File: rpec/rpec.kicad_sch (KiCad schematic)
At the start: 31 parts, among them J1 GPIO, J10 Conn_02x04_Odd_Even, J11 Conn_02x04_Odd_Even, J12 Conn_02x03_Odd_Even, J2 Conn_01x02_Pin, J3 Conn_01x03_Pin, J4 Conn_02x03_Odd_Even, J5 Conn_01x04_Male, J6 Conn_01x04_Male, J7 Conn_01x03_Pin, J8 Conn_01x03_Pin, J9 Conn_01x04_Pin, M1 Fan, U1 CAT24C256, U2 PCF8563T, U3 MCP3428x-xSL, Y1 Crystal_GND3

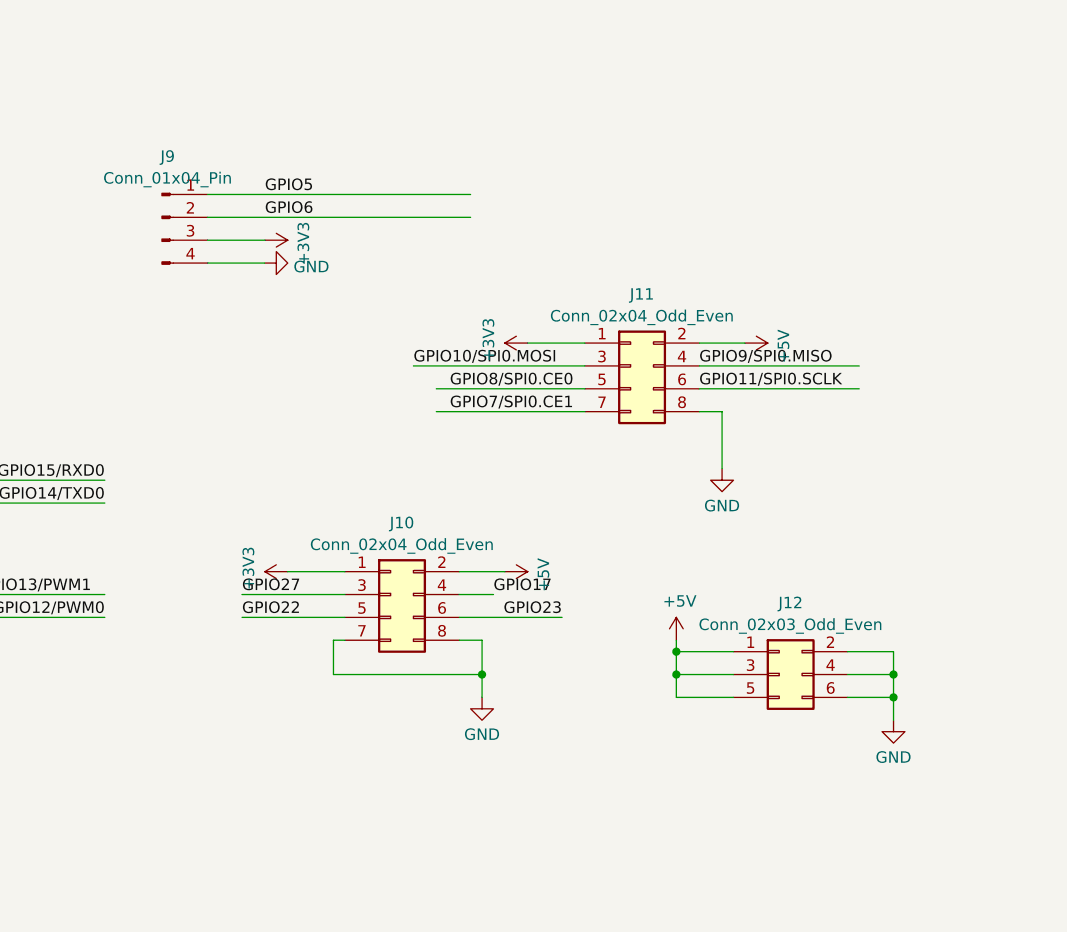
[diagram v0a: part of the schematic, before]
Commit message: rpec: schematic cosmetic fixes
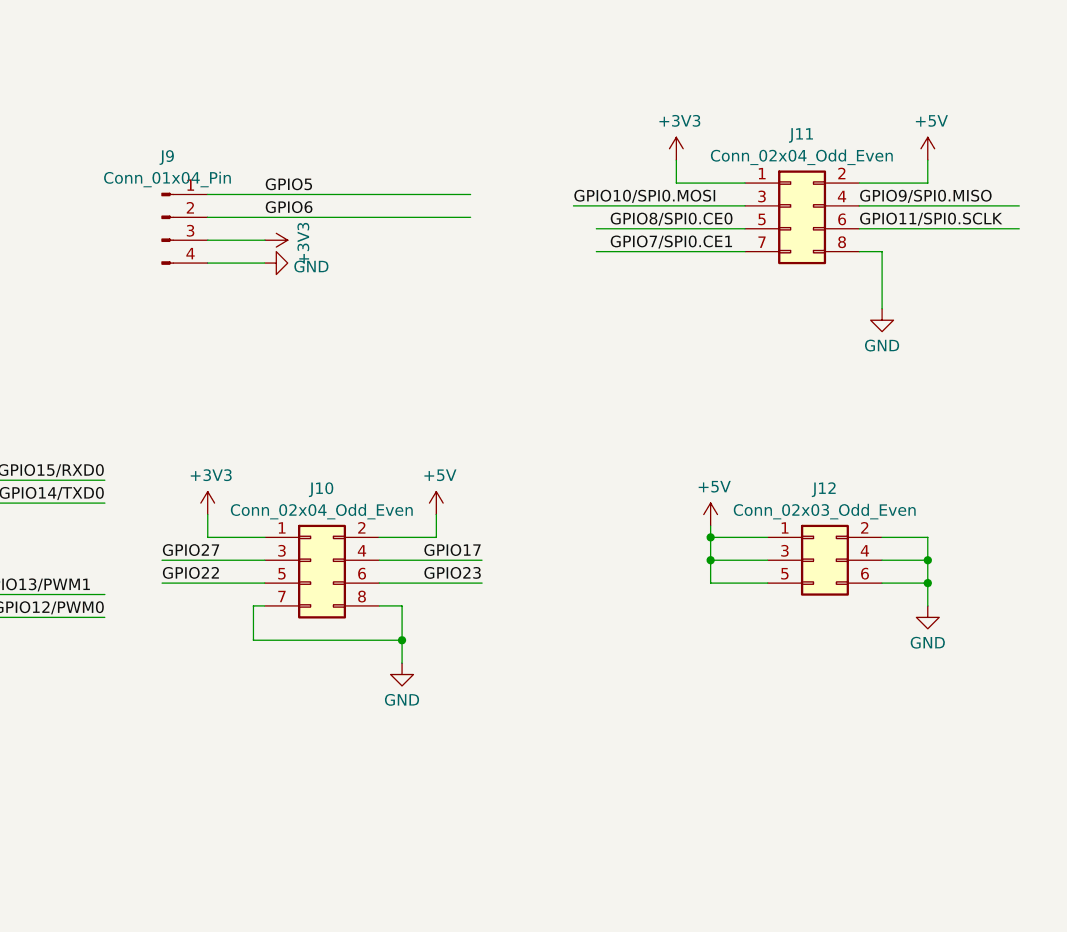
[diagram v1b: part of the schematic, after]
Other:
- title: (none) -> Raspberry Pi Essential Connectivity hat
- moved on the sheet: J10, J11, J12

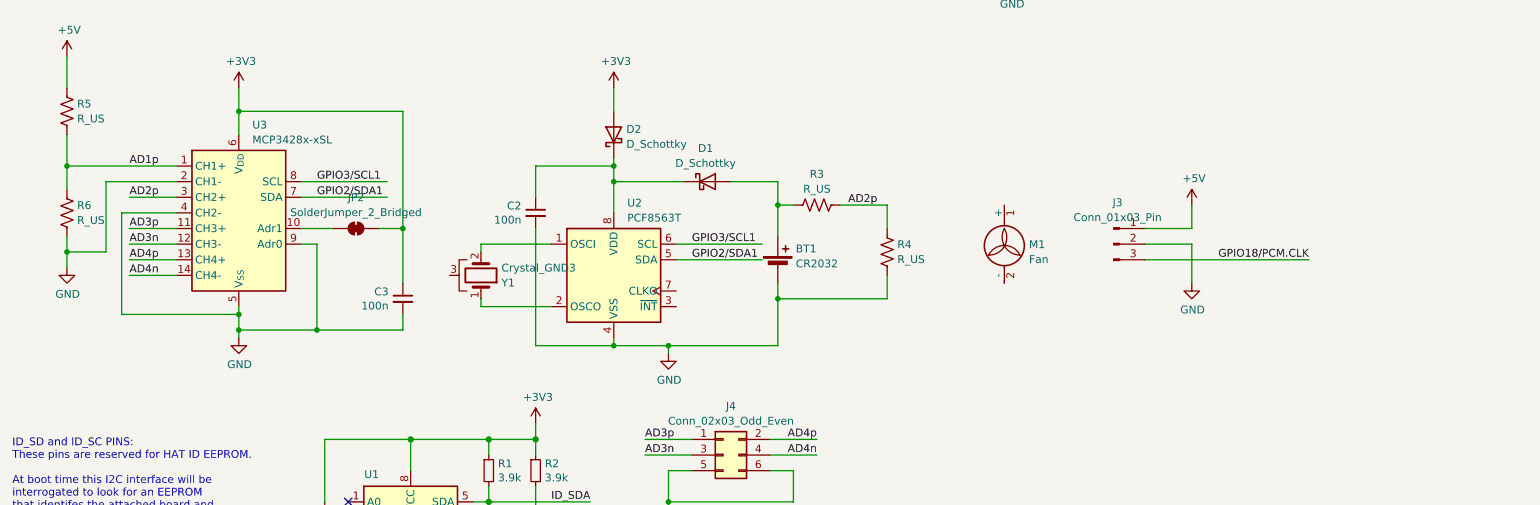
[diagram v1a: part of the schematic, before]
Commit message: rpec: r1.1 (WIP)
 - Add Pi 5-compatible fan header
 - Move RTC components and use SMD crystal
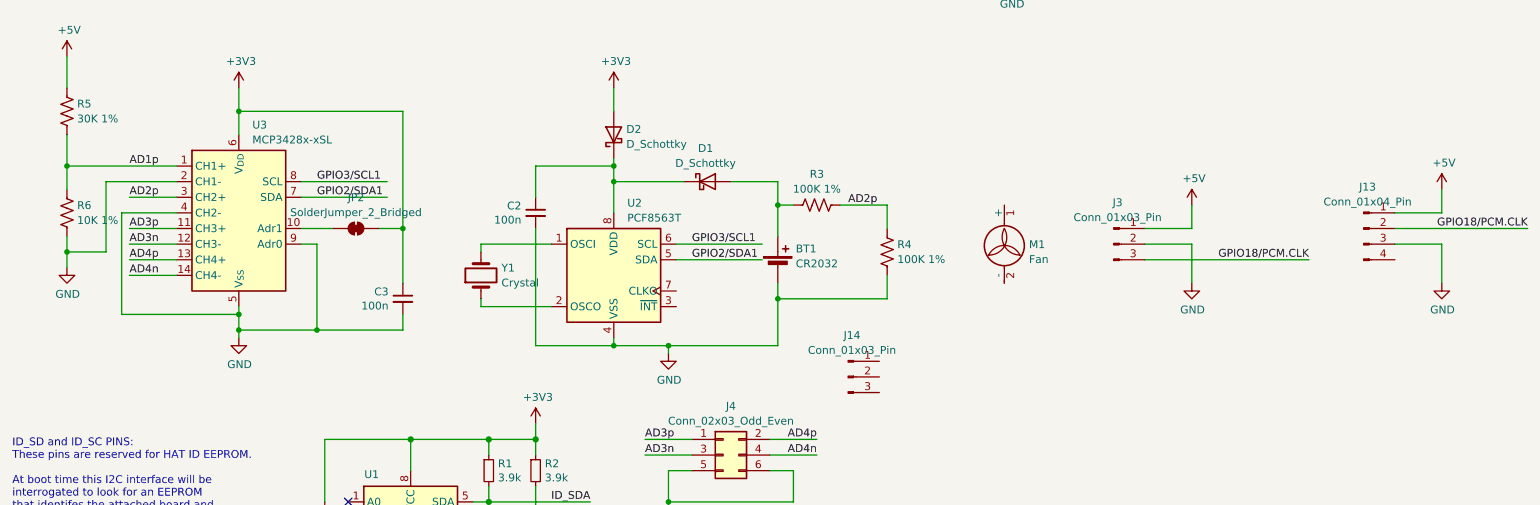
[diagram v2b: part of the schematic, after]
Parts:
- removed Y1: Crystal_GND3, Crystal:Crystal_AT310_D3.0mm_L10.0mm_Horizontal_1EP_style1, symbol Device:Crystal_GND3
- added J13: Conn_01x04_Pin, Connector_JST:JST_SH_BM04B-SRSS-TB_1x04-1MP_P1.00mm_Vertical, symbol Connector:Conn_01x04_Pin
- added J14: Conn_01x03_Pin, Connector_JST:JST_PH_B3B-PH-K_1x03_P2.00mm_Vertical, symbol Connector:Conn_01x03_Pin
- added Y1: Crystal, Crystal:Crystal_SMD_3215-2Pin_3.2x1.5mm, symbol Device:Crystal
- D1, D2: footprint Diode_SMD:D_MiniMELF_Handsoldering -> Diode_SMD:D_MiniMELF
- R3, R4: value R_US -> 100K 1%
- R5: value R_US -> 30K 1%
- R6: value R_US -> 10K 1%
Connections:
- net +5V: now also J13.1 (Pin_1)
- net GND: now also J13.3 (Pin_3)
- net GPIO18/PCM.CLK: now also J13.2 (Pin_2)
- net at U2.2 (OSCO): now also Y1.1
- net at U2.1 (OSCI): now also Y1.2
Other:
- company: (none) -> © 2024 Stephen A. Cavilia, CC BY-SA

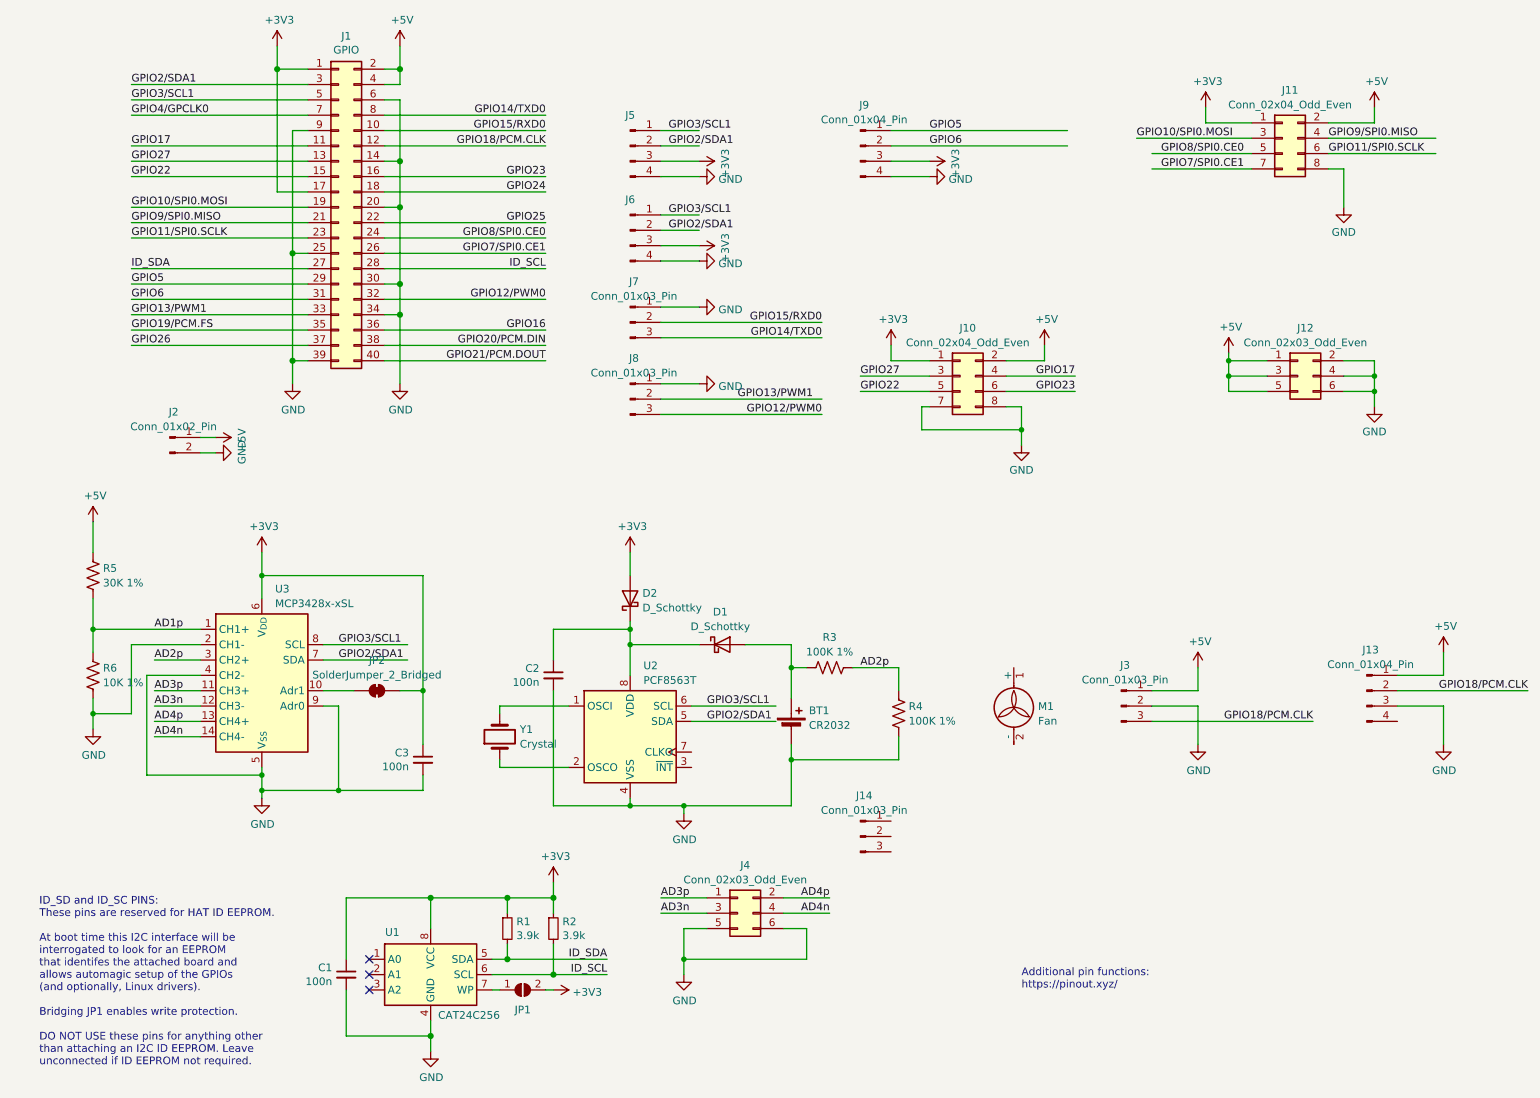
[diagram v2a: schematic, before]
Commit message: rpec: r1.1
 - Connect Pi 5 fan header
 - RTC voltage header
 - Header for Alternate ADC 1/2 inputs
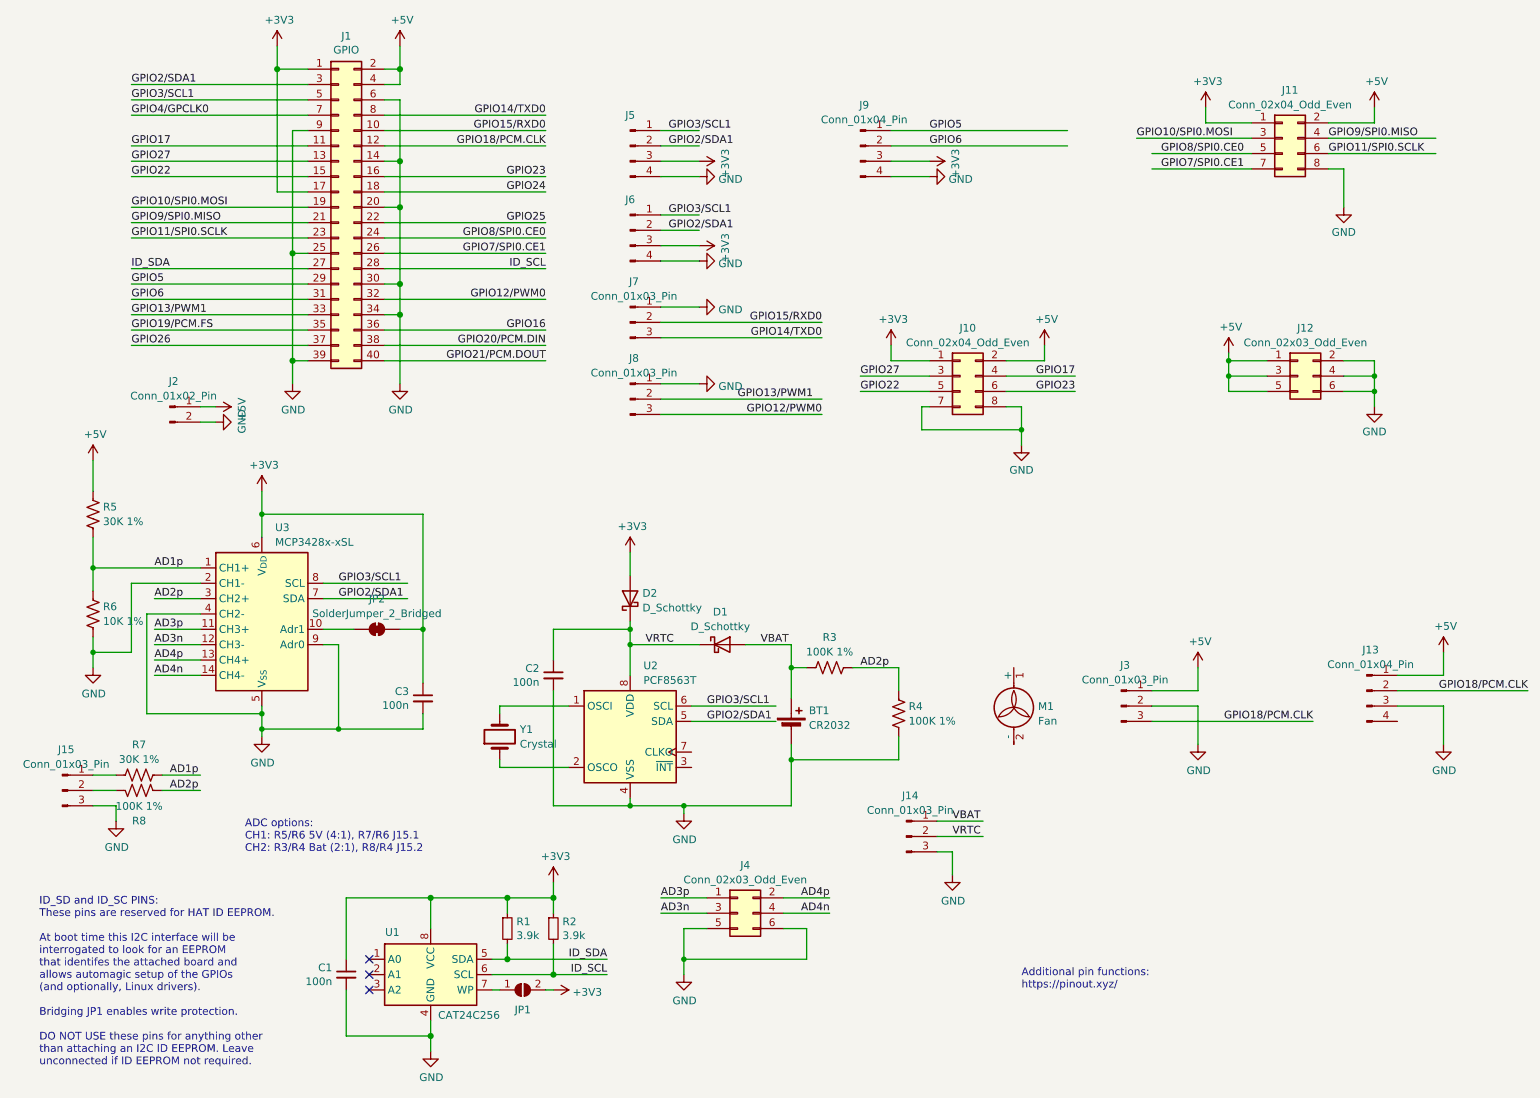
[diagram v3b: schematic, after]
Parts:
- added J15: Conn_01x03_Pin, Connector_PinHeader_2.54mm:PinHeader_1x03_P2.54mm_Vertical, symbol Connector:Conn_01x03_Pin
- added R7: 30K 1%, Resistor_SMD:R_0805_2012Metric_Pad1.20x1.40mm_HandSolder, symbol Device:R_US
- added R8: 100K 1%, Resistor_SMD:R_0805_2012Metric_Pad1.20x1.40mm_HandSolder, symbol Device:R_US
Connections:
- net AD1p: now also R7.1
- net AD2p: now also R8.1
- net GND: now also J14.3 (Pin_3), J15.3 (Pin_3)
- net VRTC: now reaches C2.1, D1.1 (K), D2.1 (K), U2.8 (VDD)
- net VRTC: now also J14.2 (Pin_2)
- net VBAT: now reaches BT1.1 (+), D1.2 (A), R3.1
- net VBAT: now also J14.1 (Pin_1)
- new net: J15.2 (Pin_2), R8.2
- new net: J15.1 (Pin_1), R7.2
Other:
- note added: "ADC options: CH1: R5/R6 5V (4:1), R7/R6 J15.1 CH2: R3/R4 Bat (2:1), R8/R4 J15.2"
- moved on the sheet: C3, J14, J2, JP2, R5, R6, U3
